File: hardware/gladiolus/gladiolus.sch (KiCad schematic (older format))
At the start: 75 parts, among them J1 NEIGHBOR1, J2 NEIGHBOR2, J7 BONUS_ROW

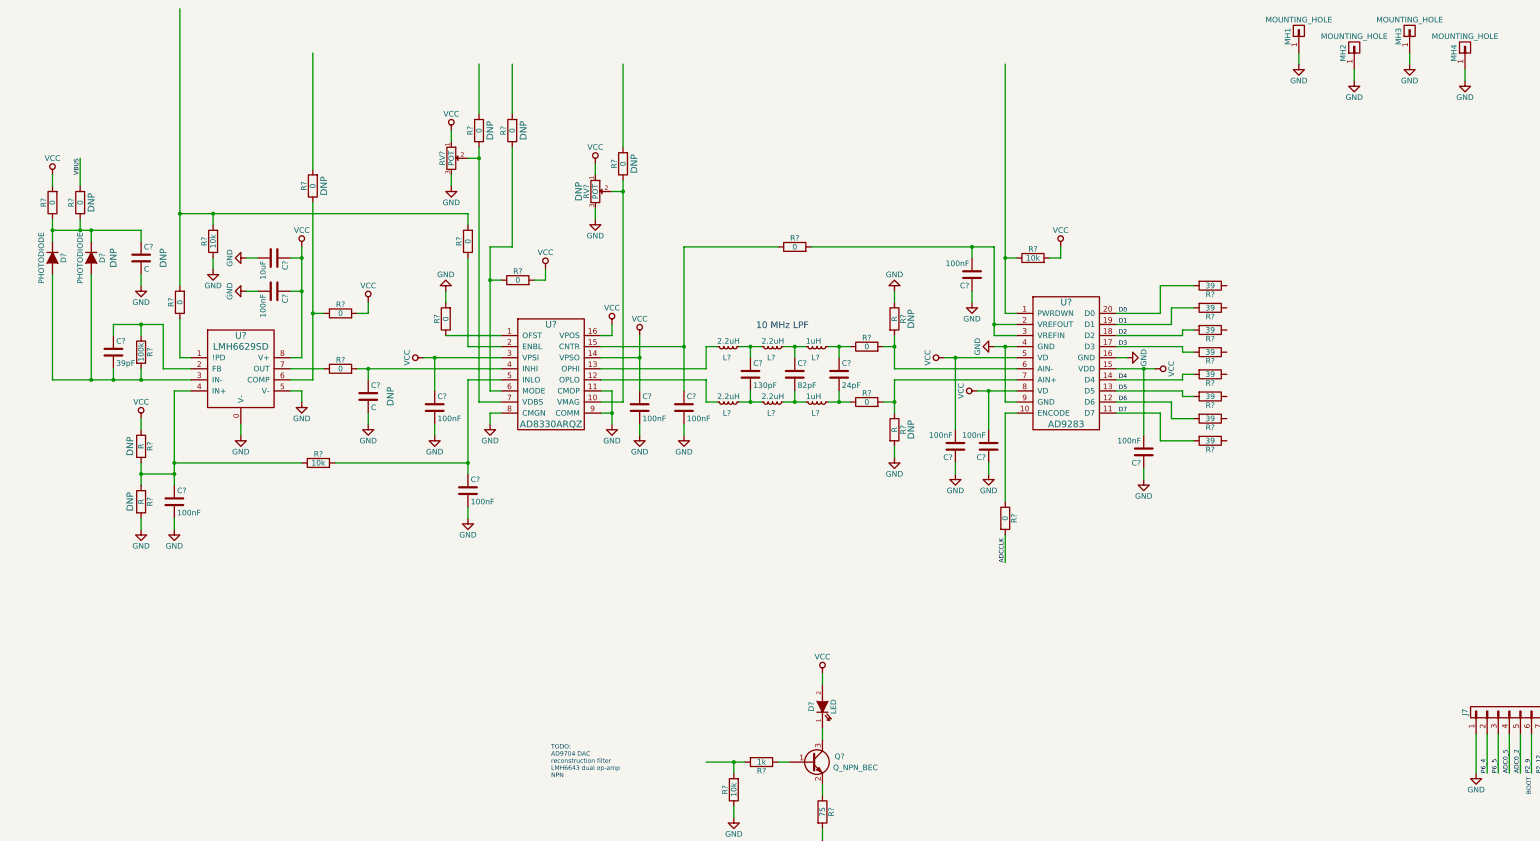
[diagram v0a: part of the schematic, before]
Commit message: replaced LMH6629 with THS4520 for easier interface to AD8330
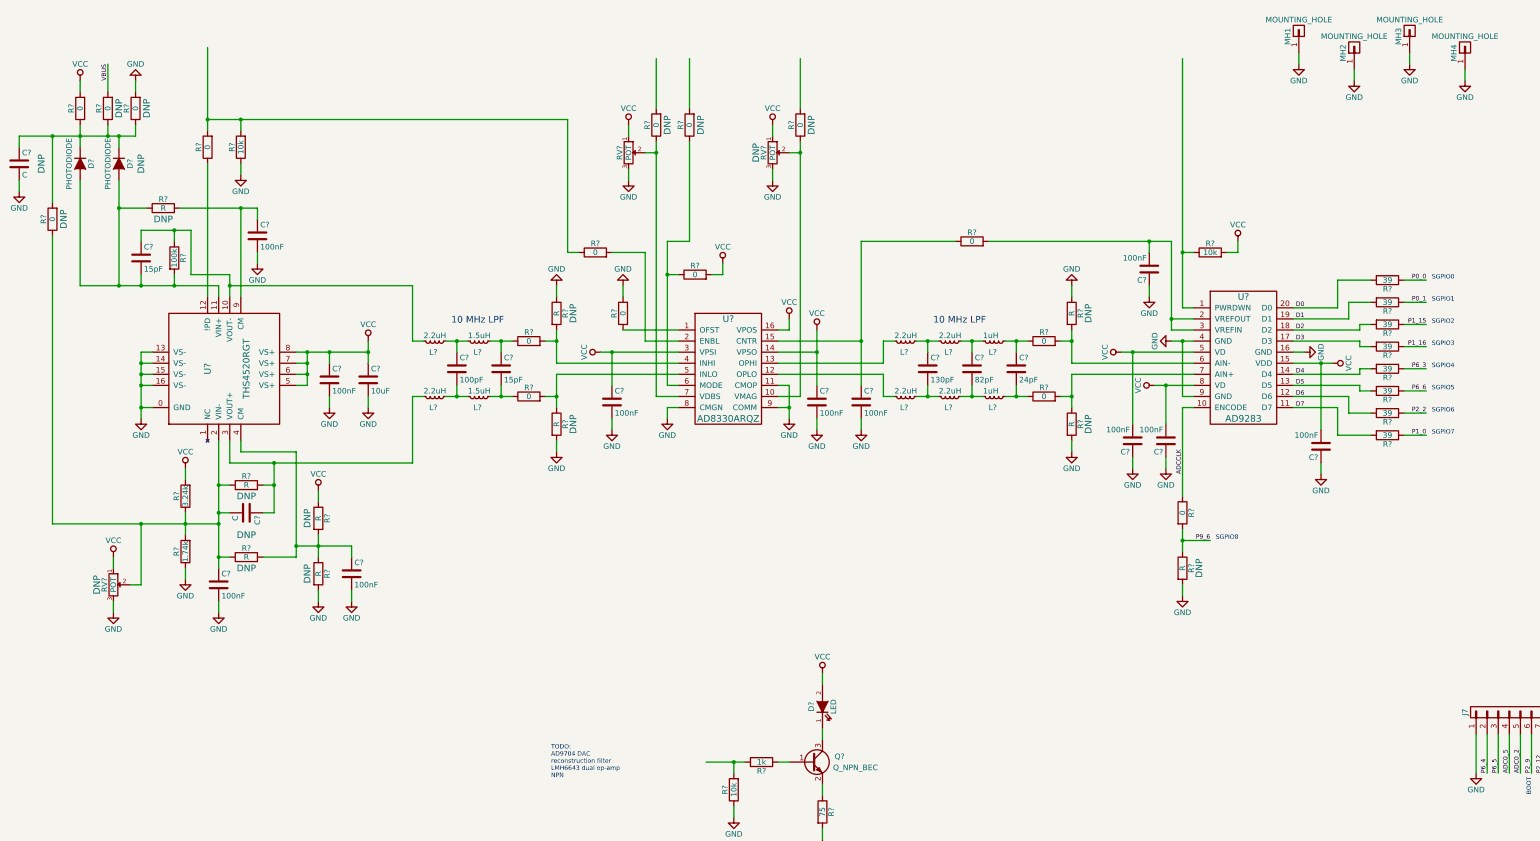
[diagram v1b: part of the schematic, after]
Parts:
- removed C?: 39pF, symbol C
- removed C?: C, symbol C
- removed C?: 100nF, symbol C
- removed R? (x2): R, symbol R
- removed R? (x3): 0, symbol R
- removed R?: 10k, symbol R
- removed U?: LMH6629SD, symbol LMH6629SD
- added C? (x2): 100nF, symbol C
- added C?: C, symbol C
- added C?: 100pF, symbol C
- added C? (x2): 15pF, symbol C
- added L? (x2): 2.2uH, symbol L_Small
- added L? (x2): 1.5uH, symbol L_Small
- added R? (x4): 0, symbol R
- added R? (x8): R, symbol R
- added R?: 1.74k, symbol R
- added R?: 3.24k, symbol R
- added RV?: POT, symbol POT
- added U?: THS4520RGT, symbol THS4520RGT
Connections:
- net ADCCLK: now also R?.1, U?.10 (ENCODE); no longer R?.2
- net GND: now also C?.2, C?.2, R?.1, R?.1, R?.2, R?.2, R?.2, R?.2, RV?.3, U?.0 (GND), U?.13 (VS-), U?.14 (VS-), U?.15 (VS-), U?.16 (VS-)
- net P0_0: now also R?.1
- net P0_1: now also R?.1
- net P1_0: now also R?.1
- net P1_15: now also R?.1
- net P1_16: now also R?.1
- net P2_2: now also R?.1
- net P6_3: now also R?.1
- net P6_6: now also R?.1
- net P9_6: now also R?.2, R?.1
- net VCC: now also R?.1, R?.2, RV?.1, U?.5 (VS+), U?.6 (VS+), U?.7 (VS+), U?.8 (VS+)
- net at C?.1, D?.1 (K), D?.1 (K)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: now also R?.1, R?.2
- net at D?.2 (A), D?.2 (A), R?.2: now also C?.2, R?.1, U?.11 (VIN+)
- net at R?.1: now also C?.1, L?.2, U?.10 (VOUT-)
- net at U?.4 (INHI): now also R?.2, R?.2
- net at U?.2 (ENBL): now also R?.2; no longer R?.1
- net at U?.5 (INLO): now also R?.1, R?.2
- net at C?.1: now also C?.2, R?.1, R?.1, R?.1, R?.1, R?.2, RV?.2, U?.2 (VIN-)
- net at R?.2, R?.2: now also R?.1; no longer R?.2
- net at R?.1: now also U?.12 (!PD)
- new net: C?.1, L?.2, R?.2, U?.3 (VOUT+)
- new net: C?.1, R?.1, R?.2, R?.2, U?.4 (CM)
- new net: C?.1, R?.2, U?.9 (CM)
- new net: C?.1, L?.1, L?.2
- new net: C?.1, L?.1, R?.1
- new net: C?.2, L?.1, L?.2
- new net: C?.2, L?.1, R?.1
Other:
- note added: "SGPIO0"
- note added: "SGPIO1"
- note added: "SGPIO2"
- note added: "SGPIO3"
- note added: "SGPIO4"
- note added: "SGPIO5"
- note added: "SGPIO6"
- note added: "SGPIO7"
- note added: "SGPIO8"
- moved on the sheet: C?, D?, L?, R?, RV?, U?

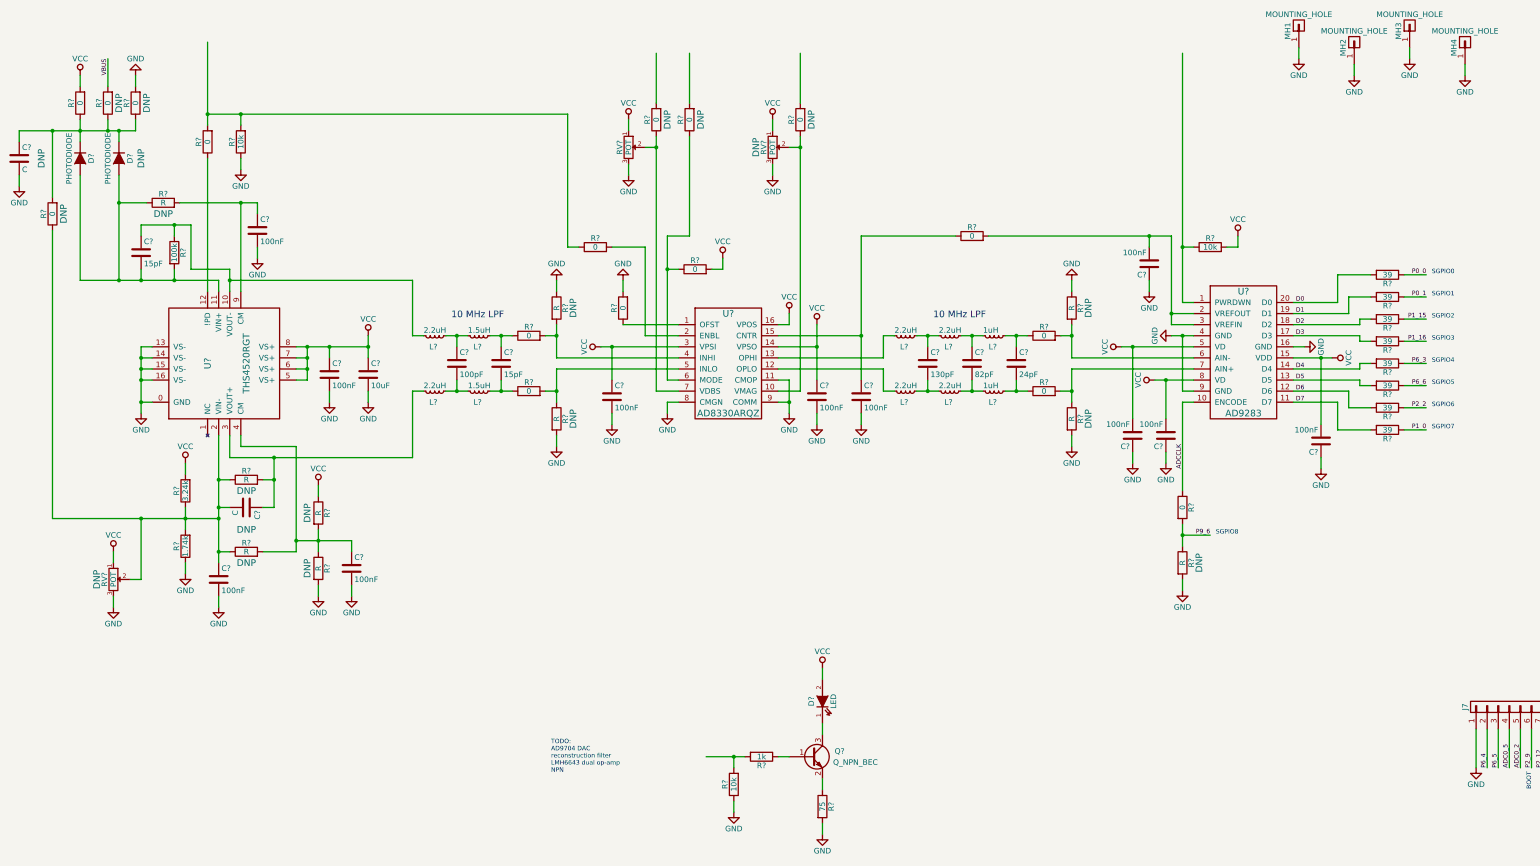
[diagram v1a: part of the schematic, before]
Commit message: Gladiolus: finished neighbor pin selection
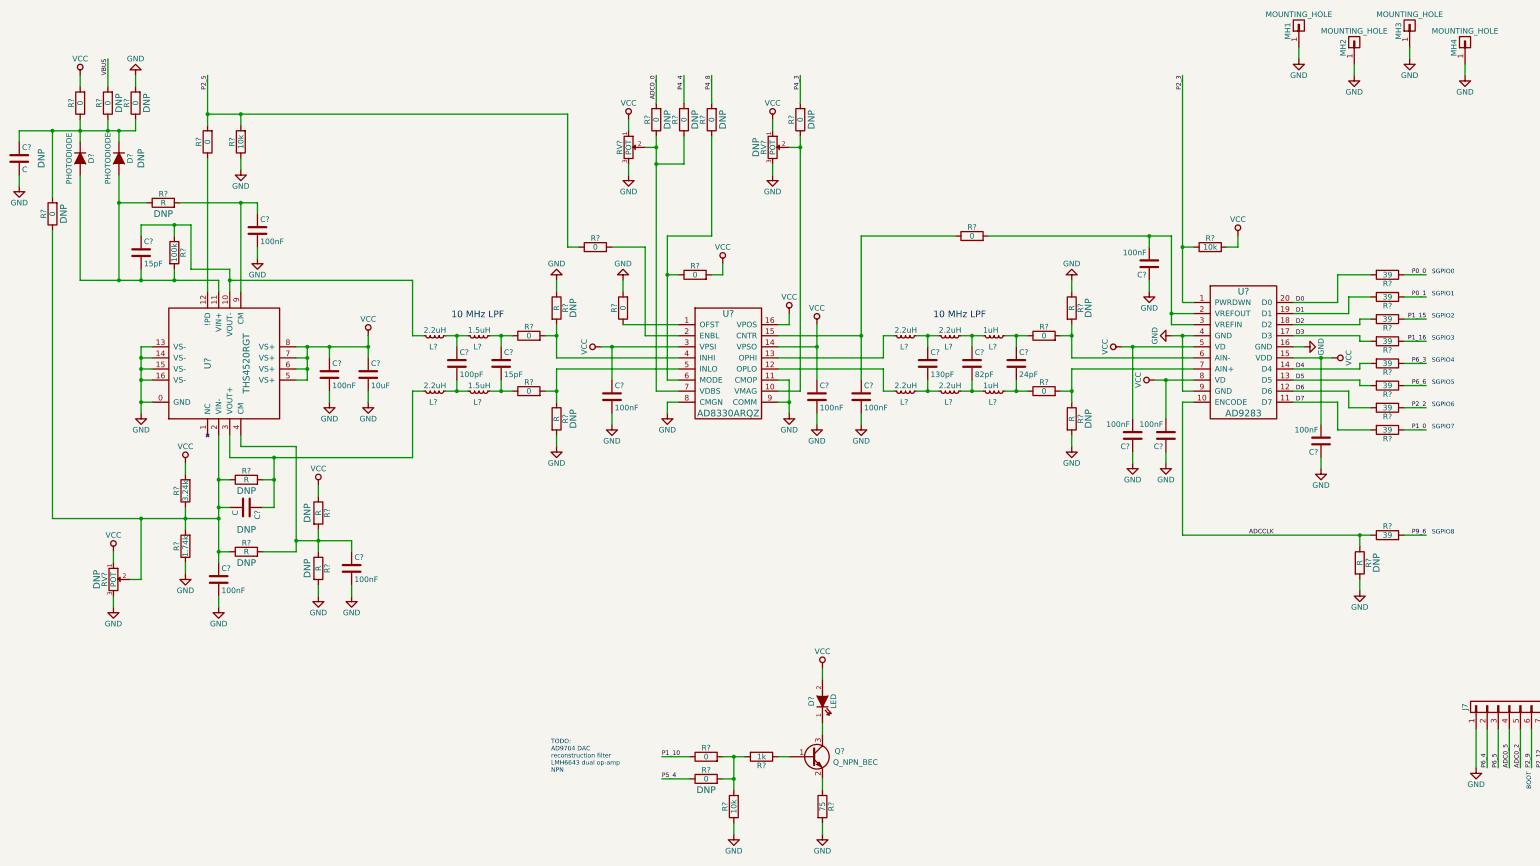
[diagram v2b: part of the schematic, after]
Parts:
- removed R?: 0, symbol R
- added R? (x3): 0, symbol R
- added R?: 39, symbol R
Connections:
- net ADC0_0: now also R?.2
- net ADCCLK: now also R?.1, R?.1
- net P1_10: now also R?.1
- net P2_3: now also R?.1, U?.1 (PWRDWN)
- net P2_5: now also R?.1, R?.2, R?.2
- net P4_3: now also R?.2
- net P4_4: now also R?.2
- net P4_8: now also R?.2
- net P5_4: now also R?.1
- net P9_6: now also R?.2; no longer R?.1
- net at R?.1, RV?.2, U?.7 (VDBS): now also R?.1
- net at R?.2, R?.2: now also R?.2, R?.2
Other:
- moved on the sheet: R?
